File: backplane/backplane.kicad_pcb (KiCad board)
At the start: 2 copper layers, 150 x 150 mm, 12 parts

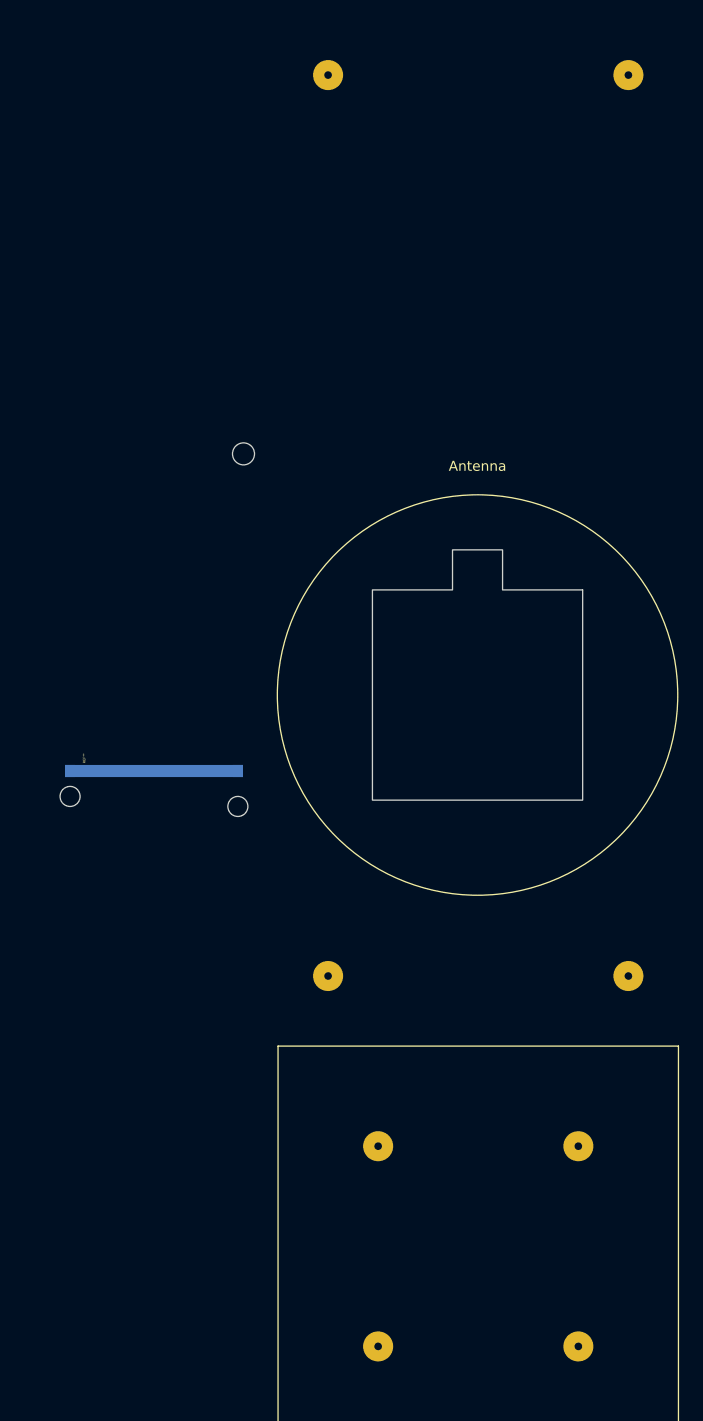
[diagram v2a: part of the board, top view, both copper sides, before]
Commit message: Moved transformer slot to be tangent with antenna slot
Adjusted slot so that it lines up with where the antenna wire ends for
nice flow for wire to feed through.
Also changed mount holes to be full 3mm mechanical drill holes for the
following footprints:
- Handle Clamp
- Phone Holder
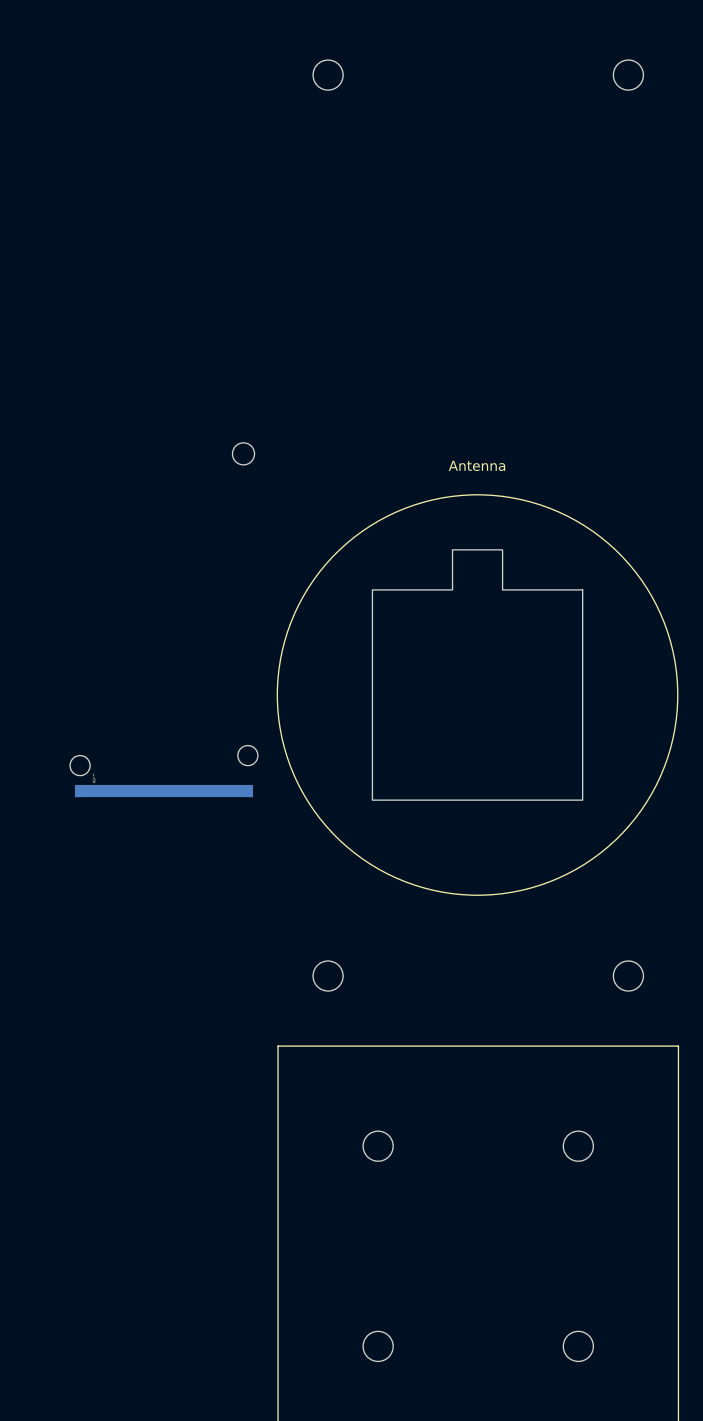
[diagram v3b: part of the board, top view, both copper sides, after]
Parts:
- moved REF** 2.24 mm to (60.0, 115.0)
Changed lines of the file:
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@@
     (uvia_drill 0.1)
+  )
+  (module DxWiFi:Handle-Clamp (layer F.Cu)
+    (at 77.86 180.48)
+    (fp_text reference Handle-Clamp (at 20.32 -3.81) (layer F.SilkS) hide
+      (effects (font (size 1 1) (thickness 0.15)))
+    )
+    (fp_text value Handle-Clamp (at 20.32 -1.27) (layer F.SilkS)
+      (effects (font (size 1 1) (thickness 0.15)))
+    )
+    (fp_line (start 0 -40) (end 0 0) (layer B.SilkS) (width 0.12))
+    (fp_line (start 0 0) (end 40 0) (layer B.SilkS) (width 0.12))
+    (fp_line (start 40 0) (end 40 -40) (layer B.SilkS) (width 0.12))
+    (fp_line (start 40 -40) (end 0 -40) (layer B.SilkS) (width 0.12))
+    (fp_text user Handle-Clamp (at 20.32 -1.27) (layer B.SilkS)
+      (effects (font (size 1 1) (thickness 0.15)))
+    )
+    (fp_line (start 0 -40) (end 0 0) (layer F.SilkS) (width 0.12))
+    (fp_line (start 40 -40) (end 0 -40) (layer F.SilkS) (width 0.12))
+    (fp_line (start 40 0) (end 40 -40) (layer F.SilkS) (width 0.12))
+    (fp_line (start 0 0) (end 40 0) (layer F.SilkS) (width 0.12))
+    (pad "" np_thru_hole circle (at 10 -30) (size 3 3) (drill 3) (layers *.Cu *.Mask))
+    (pad "" np_thru_hole circle (at 30 -30) (size 3 3) (drill 3) (layers *.Cu *.Mask))
+    (pad "" np_thru_hole circle (at 30 -10) (size 3 3) (drill 3) (layers *.Cu *.Mask))
+    (pad "" np_thru_hole circle (at 10 -10) (size 3 3) (drill 3) (layers *.Cu *.Mask))
+  )
+  (module DxWiFi:Phone-Holder (layer F.Cu)
+    (at 67.86 138.48)
+    (fp_text reference "Phone Holder" (at 29.93 -2.59) (layer B.SilkS)
+      (effects (font (size 1 1) (thickness 0.15)))
+    )
+    (fp_text value Phone-Holder (at 30.48 -5.13) (layer B.SilkS) hide
+      (effects (font (size 1 1) (thickness 0.15)))
+    )
+    (fp_line (start 0 -90) (end 60 -90) (layer B.SilkS) (width 0.12))
+    (fp_line (start 0 -10) (end 60 -10) (layer B.SilkS) (width 0.12))
+    (fp_line (start 0 -100) (end 0 0) (layer B.SilkS) (width 0.12))
+    (fp_line (start 60 -100) (end 0 -100) (layer B.SilkS) (width 0.12))
+    (fp_line (start 60 0) (end 60 -100) (layer B.SilkS) (width 0.12))
+    (fp_line (start 0 0) (end 60 0) (layer B.SilkS) (width 0.12))
+    (pad "" np_thru_hole circle (at 15 -95) (size 3 3) (drill 3) (layers *.Cu *.Mask))
+    (pad "" np_thru_hole circle (at 45 -95) (size 3 3) (drill 3) (layers *.Cu *.Mask))
+    (pad "" np_thru_hole circle (at 45 -5) (size 3 3) (drill 3) (layers *.Cu *.Mask))
+    (pad "" np_thru_hole circle (at 15 -5) (size 3 3) (drill 3) (layers *.Cu *.Mask))
+  )
+  (module muwave_stub (layer F.Cu)
+    (at 60 115 270)
+    (fp_text reference REF** (at -1.27 0.5 90) (layer F.SilkS)
+      (effects (font (size 0.25 0.25) (thickness 0.05)))
+    )
+    (fp_text value muwave_stub (at 0 -0.5 90) (layer F.Fab)
+      (effects (font (size 0.25 0.25) (thickness 0.05)))
+    )
+    (pad "" np_thru_hole circle (at -2.54 1.915 270) (size 2 2) (drill 2) (layers *.Cu *.Mask))
+    (pad "" np_thru_hole roundrect (at -3.54 -14.8473 270) (size 4 2) (drill 2) (layers *.Cu) (roundrect_rratio 0.25)
+      (clearance 0.5))
+    (pad 2 smd rect (at 0 1.915 270) (size 1.20938 1) (layers B.Cu B.Mask))
+    (pad 2 smd rect (at 0 -14.8473 270) (size 1.20938 1) (layers B.Cu B.Mask))
+    (pad 1 smd rect (at 0 0 270) (size 0.25 0.25) (layers B.Cu))
+    (pad 1 smd rect (at 0 -6.46615 270) (size 1.20938 17.7623) (layers B.Cu)
+      (clearance 12.6))
   )
   (module DxWiFi:string_mount (layer F.Cu)
@@
     )
     (pad "" np_thru_hole circle (at 0 1.27) (size 2 2) (drill 2) (layers *.Cu *.Mask))
-  )
-  (module muwave_stub (layer F.Cu)
-    (at 59 113 270)
-    (fp_text reference REF** (at -1.27 0.5 270) (layer F.SilkS)
-      (effects (font (size 0.25 0.25) (thickness 0.05)))
-    )
-    (fp_text value muwave_stub (at 0 -0.5 270) (layer F.Fab)
-      (effects (font (size 0.25 0.25) (thickness 0.05)))
-    )
-    (pad 1 smd rect (at 0 -6.46615 270) (size 1.20938 17.7623) (layers B.Cu)
-      (clearance 12.6))
-    (pad 1 smd rect (at 0 0 270) (size 0.25 0.25) (layers B.Cu))
-    (pad 2 smd rect (at 0 -14.8473 270) (size 1.20938 1) (layers B.Cu B.Mask))
-    (pad 2 smd rect (at 0 1.915 270) (size 1.20938 1) (layers B.Cu B.Mask))
-    (pad "" np_thru_hole roundrect (at 3.54 -14.8473 270) (size 4 2) (drill 2) (layers *.Cu) (roundrect_rratio 0.25)
-      (clearance 0.5))
-    (pad "" np_thru_hole circle (at 2.54 1.915 270) (size 2 2) (drill 2) (layers *.Cu *.Mask))
   )
   (module DxWiFi:Atheros (layer F.Cu)
@@
     (fp_circle (center 0 0) (end 20 0) (layer F.SilkS) (width 0.12))
   )
-  (module DxWiFi:Phone-Holder (layer F.Cu)
-    (at 67.86 138.48)
-    (fp_text reference "Phone Holder" (at 29.93 -2.59) (layer B.SilkS)
-      (effects (font (size 1 1) (thickness 0.15)))
-    )
-    (fp_text value Phone-Holder (at 30.48 -5.13) (layer B.SilkS) hide
-      (effects (font (size 1 1) (thickness 0.15)))
-    )
-    (fp_line (start 0 -90) (end 60 -90) (layer B.SilkS) (width 0.12))
-    (fp_line (start 0 -10) (end 60 -10) (layer B.SilkS) (width 0.12))
-    (fp_line (start 0 -100) (end 0 0) (layer B.SilkS) (width 0.12))
-    (fp_line (start 60 -100) (end 0 -100) (layer B.SilkS) (width 0.12))
-    (fp_line (start 60 0) (end 60 -100) (layer B.SilkS) (width 0.12))
-    (fp_line (start 0 0) (end 60 0) (layer B.SilkS) (width 0.12))
-    (pad 4 thru_hole circle (at 15 -95) (size 3 3) (drill 0.762) (layers *.Cu *.Mask))
-    (pad 3 thru_hole circle (at 45 -95) (size 3 3) (drill 0.762) (layers *.Cu *.Mask))
-    (pad 2 thru_hole circle (at 45 -5) (size 3 3) (drill 0.762) (layers *.Cu *.Mask))
-    (pad 1 thru_hole circle (at 15 -5) (size 3 3) (drill 0.762) (layers *.Cu *.Mask))
-  )
-  (module DxWiFi:Handle-Clamp (layer F.Cu)
-    (at 77.86 180.48)
-    (fp_text reference Handle-Clamp (at 20.32 -3.81) (layer F.SilkS) hide
-      (effects (font (size 1 1) (thickness 0.15)))
-    )
-    (fp_text value Handle-Clamp (at 20.32 -1.27) (layer F.SilkS)
-      (effects (font (size 1 1) (thickness 0.15)))
-    )
-    (fp_line (start 0 -40) (end 0 0) (layer B.SilkS) (width 0.12))
-    (fp_line (start 0 0) (end 40 0) (layer B.SilkS) (width 0.12))
-    (fp_line (start 40 0) (end 40 -40) (layer B.SilkS) (width 0.12))
-    (fp_line (start 40 -40) (end 0 -40) (layer B.SilkS) (width 0.12))
-    (fp_text user Handle-Clamp (at 20.32 -1.27) (layer B.SilkS)
-      (effects (font (size 1 1) (thickness 0.15)))
-    )
-    (fp_line (start 0 -40) (end 0 0) (layer F.SilkS) (width 0.12))
-    (fp_line (start 40 -40) (end 0 -40) (layer F.SilkS) (width 0.12))
-    (fp_line (start 40 0) (end 40 -40) (layer F.SilkS) (width 0.12))
-    (fp_line (start 0 0) (end 40 0) (layer F.SilkS) (width 0.12))
-    (pad 4 thru_hole circle (at 10 -30) (size 3 3) (drill 0.762) (layers *.Cu *.Mask))
-    (pad 3 thru_hole circle (at 30 -30) (size 3 3) (drill 0.762) (layers *.Cu *.Mask))
-    (pad 2 thru_hole circle (at 30 -10) (size 3 3) (drill 0.762) (layers *.Cu *.Mask))
-    (pad 1 thru_hole circle (at 10 -10) (size 3 3) (drill 0.762) (layers *.Cu *.Mask))
-  )
   (module DxWiFi:microstrip (layer F.Cu)

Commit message: Added ground planes and vias
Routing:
- net (no net): vias 0 -> 62
- added copper zone on B.Cu, net (none)
- added copper zone on F.Cu, net (none)
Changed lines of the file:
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@@
     (thickness 1.6)
     (drawings 4)
-    (tracks 0)
+    (tracks 62)
     (zones 0)
     (modules 12)
@@
   )
   (page A4)
+  (title_block
+    (date 2019-05-13)
+    (rev v1.1)
+  )
   (layers
-    (0 F.Cu signal)
+    (0 F.Cu signal hide)
     (31 B.Cu power)
     (32 B.Adhes user)
@@
     (mod_text_size 1 1)
     (mod_text_width 0.15)
-    (pad_size 4 2)
-    (pad_drill 2)
+    (pad_size 0.8 0.8)
+    (pad_drill 0.4)
     (pad_to_mask_clearance 0.051)
     (solder_mask_min_width 0.25)
@@
   (gr_line (start 172.86 30.48) (end 172.86 180.48) (layer Edge.Cuts) (width 0.05))
   (gr_line (start 22.86 30.48) (end 172.86 30.48) (layer Edge.Cuts) (width 0.05))
+  (via (at 167.84 175.48) (size 0.8) (drill 0.4) (layers F.Cu B.Cu) (net 0))
+  (via (at 147.84 175.48) (size 0.8) (drill 0.4) (layers F.Cu B.Cu) (net 0))
+  (via (at 127.84 175.48) (size 0.8) (drill 0.4) (layers F.Cu B.Cu) (net 0))
+  (via (at 107.84 175.48) (size 0.8) (drill 0.4) (layers F.Cu B.Cu) (net 0))
+  (via (at 87.84 175.48) (size 0.8) (drill 0.4) (layers F.Cu B.Cu) (net 0))
+  (via (at 67.84 175.48) (size 0.8) (drill 0.4) (layers F.Cu B.Cu) (net 0))
+  (via (at 47.84 175.48) (size 0.8) (drill 0.4) (layers F.Cu B.Cu) (net 0))
+  (via (at 27.84 175.48) (size 0.8) (drill 0.4) (layers F.Cu B.Cu) (net 0))
+  (via (at 167.84 155.48) (size 0.8) (drill 0.4) (layers F.Cu B.Cu) (net 0))
+  (via (at 147.84 155.48) (size 0.8) (drill 0.4) (layers F.Cu B.Cu) (net 0))
+  (via (at 127.84 155.48) (size 0.8) (drill 0.4) (layers F.Cu B.Cu) (net 0))
+  (via (at 107.84 155.48) (size 0.8) (drill 0.4) (layers F.Cu B.Cu) (net 0))
+  (via (at 87.84 155.48) (size 0.8) (drill 0.4) (layers F.Cu B.Cu) (net 0))
+  (via (at 67.84 155.48) (size 0.8) (drill 0.4) (layers F.Cu B.Cu) (net 0))
+  (via (at 47.84 155.48) (size 0.8) (drill 0.4) (layers F.Cu B.Cu) (net 0))
+  (via (at 27.84 155.48) (size 0.8) (drill 0.4) (layers F.Cu B.Cu) (net 0))
+  (via (at 167.84 135.48) (size 0.8) (drill 0.4) (layers F.Cu B.Cu) (net 0))
+  (via (at 147.84 135.48) (size 0.8) (drill 0.4) (layers F.Cu B.Cu) (net 0))
+  (via (at 127.84 135.48) (size 0.8) (drill 0.4) (layers F.Cu B.Cu) (net 0))
+  (via (at 107.84 135.48) (size 0.8) (drill 0.4) (layers F.Cu B.Cu) (net 0))
+  (via (at 87.84 135.48) (size 0.8) (drill 0.4) (layers F.Cu B.Cu) (net 0))
+  (via (at 67.84 135.48) (size 0.8) (drill 0.4) (layers F.Cu B.Cu) (net 0))
+  (via (at 47.84 135.48) (size 0.8) (drill 0.4) (layers F.Cu B.Cu) (net 0))
+  (via (at 27.84 135.48) (size 0.8) (drill 0.4) (layers F.Cu B.Cu) (net 0))
+  (via (at 167.84 115.48) (size 0.8) (drill 0.4) (layers F.Cu B.Cu) (net 0))
+  (via (at 147.84 115.48) (size 0.8) (drill 0.4) (layers F.Cu B.Cu) (net 0))
+  (via (at 127.84 115.48) (size 0.8) (drill 0.4) (layers F.Cu B.Cu) (net 0))
+  (via (at 27.84 115.48) (size 0.8) (drill 0.4) (layers F.Cu B.Cu) (net 0))
+  (via (at 147.84 95.48) (size 0.8) (drill 0.4) (layers F.Cu B.Cu) (net 0))
+  (via (at 127.84 95.48) (size 0.8) (drill 0.4) (layers F.Cu B.Cu) (net 0))
+  (via (at 67.84 95.48) (size 0.8) (drill 0.4) (layers F.Cu B.Cu) (net 0))
+  (via (at 47.84 95.48) (size 0.8) (drill 0.4) (layers F.Cu B.Cu) (net 0))
+  (via (at 27.84 95.48) (size 0.8) (drill 0.4) (layers F.Cu B.Cu) (net 0))
+  (via (at 167.84 75.48) (size 0.8) (drill 0.4) (layers F.Cu B.Cu) (net 0))
+  (via (at 147.84 75.48) (size 0.8) (drill 0.4) (layers F.Cu B.Cu) (net 0))
+  (via (at 127.84 75.48) (size 0.8) (drill 0.4) (layers F.Cu B.Cu) (net 0))
+  (via (at 107.84 75.48) (size 0.8) (drill 0.4) (layers F.Cu B.Cu) (net 0))
+  (via (at 87.84 75.48) (size 0.8) (drill 0.4) (layers F.Cu B.Cu) (net 0))
+  (via (at 67.84 75.48) (size 0.8) (drill 0.4) (layers F.Cu B.Cu) (net 0))
+  (via (at 47.84 75.48) (size 0.8) (drill 0.4) (layers F.Cu B.Cu) (net 0))
+  (via (at 27.84 75.48) (size 0.8) (drill 0.4) (layers F.Cu B.Cu) (net 0))
+  (via (at 167.84 55.48) (size 0.8) (drill 0.4) (layers F.Cu B.Cu) (net 0))
+  (via (at 147.84 55.48) (size 0.8) (drill 0.4) (layers F.Cu B.Cu) (net 0))
+  (via (at 127.84 55.48) (size 0.8) (drill 0.4) (layers F.Cu B.Cu) (net 0))
+  (via (at 107.84 55.48) (size 0.8) (drill 0.4) (layers F.Cu B.Cu) (net 0))
+  (via (at 87.84 55.48) (size 0.8) (drill 0.4) (layers F.Cu B.Cu) (net 0))
+  (via (at 67.84 55.48) (size 0.8) (drill 0.4) (layers F.Cu B.Cu) (net 0))
+  (via (at 47.84 55.48) (size 0.8) (drill 0.4) (layers F.Cu B.Cu) (net 0))
+  (via (at 27.84 55.48) (size 0.8) (drill 0.4) (layers F.Cu B.Cu) (net 0))
+  (via (at 168 39) (size 0.8) (drill 0.4) (layers F.Cu B.Cu) (net 0))
+  (via (at 147.84 35.48) (size 0.8) (drill 0.4) (layers F.Cu B.Cu) (net 0))
+  (via (at 127.84 35.48) (size 0.8) (drill 0.4) (layers F.Cu B.Cu) (net 0))
+  (via (at 107.84 35.48) (size 0.8) (drill 0.4) (layers F.Cu B.Cu) (net 0))
+  (via (at 87.84 35.48) (size 0.8) (drill 0.4) (layers F.Cu B.Cu) (net 0))
+  (via (at 67.84 35.48) (size 0.8) (drill 0.4) (layers F.Cu B.Cu) (net 0))
+  (via (at 47.84 35.48) (size 0.8) (drill 0.4) (layers F.Cu B.Cu) (net 0))
+  (via (at 27.84 35.48) (size 0.8) (drill 0.4) (layers F.Cu B.Cu) (net 0))
+  (via (at 167.84 97) (size 0.8) (drill 0.4) (layers F.Cu B.Cu) (net 0))
+  (via (at 89 119) (size 0.8) (drill 0.4) (layers F.Cu B.Cu) (net 0))
+  (via (at 85 99) (size 0.8) (drill 0.4) (layers F.Cu B.Cu) (net 0))
+  (via (at 110 92) (size 0.8) (drill 0.4) (layers F.Cu B.Cu) (net 0))
+  (via (at 112 118) (size 0.8) (drill 0.4) (layers F.Cu B.Cu) (net 0))
+  (zone (net 0) (net_name "") (layer F.Cu) (hatch none 0.508)
+    (connect_pads (clearance 0.508))
+    (min_thickness 0.254)
+    (fill yes (arc_segments 32) (thermal_gap 0.508) (thermal_bridge_width 0.508))
+    (polygon
+      (pts
+        (xy 172 31) (xy 23 31) (xy 23 180) (xy 172 180)
+      )
+    )
+  )
+  (zone (net 0) (net_name "") (layer B.Cu) (hatch edge 0.508)
+    (connect_pads (clearance 0.508))
+    (min_thickness 0.254)
+    (fill yes (arc_segments 32) (thermal_gap 0.508) (thermal_bridge_width 0.508))
+    (polygon
+      (pts
+        (xy 172 31) (xy 23 31) (xy 23 180) (xy 172 180)
+      )
+    )
+  )
 )

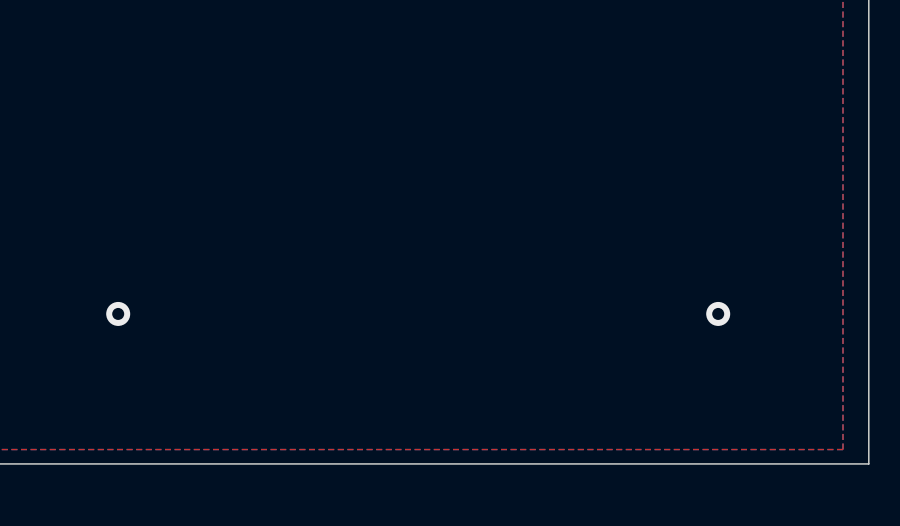
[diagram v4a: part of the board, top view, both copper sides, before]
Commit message: Connected GND planes using vias with common net
Added new footprint linked with net from two floating inductors in schematic
to associate both planes and all vias to connect everything together.
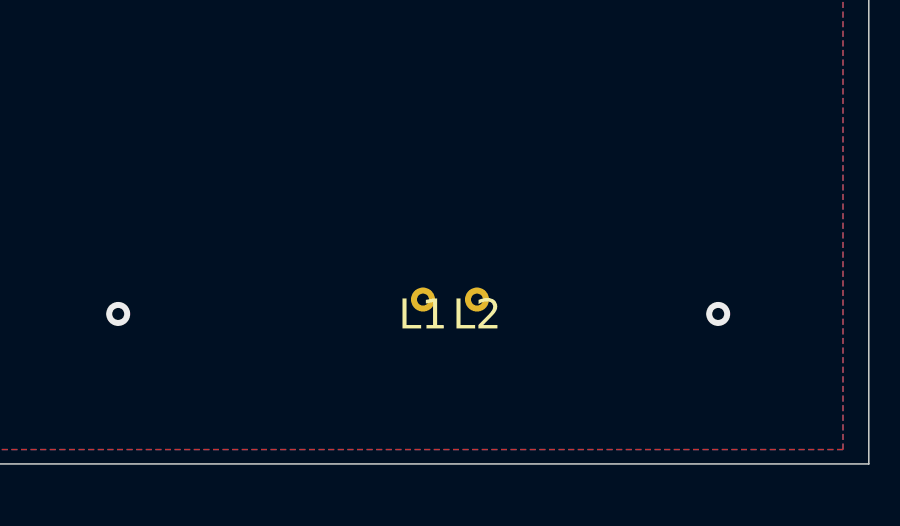
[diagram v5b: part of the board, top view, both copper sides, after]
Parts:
- added L1: L, DxWiFi:GND-pad, F.Cu at (158.0, 175.0)
- added L2: L, DxWiFi:GND-pad, F.Cu at (159.8, 175.0)
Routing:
- net Net-(L1-Pad1): vias 0 -> 62
- net (no net): vias 62 -> 0
- added copper zone on B.Cu, net Net-(L1-Pad1)
- added copper zone on F.Cu, net Net-(L1-Pad1)
- removed copper zone on B.Cu, net (none)
- removed copper zone on F.Cu, net (none)
